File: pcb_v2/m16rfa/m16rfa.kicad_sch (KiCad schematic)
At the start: 51 parts, among them J1 S16A, J10 bus_rf16_3, J2 S16A, J3 SWRDA, J5 S16A, J6 S16A, J7 S16A, J8 bus_rf16_1, J9 bus_rf16_2, U1 74LS125, U10 74LS244, U11 74LS244, U2 74LS193, U3 74LS138, U4 74LS08, U5 74LS04, U6 74LS08, U7 74LS244, U8 74LS244, U9 74LS244

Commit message: recomeçando o roteamento
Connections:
- net +5V: now also U4.12, U4.13, U5.11, U5.13, U5.5, U5.9, U6.12, U6.13
- net data_{0}: now also J8.4 (Pin_4); no longer J8.14 (Pin_14)
- net data_{1}: now also J8.3 (Pin_3); no longer J8.13 (Pin_13)
- net data_{2}: now also J8.5 (Pin_5); no longer J8.11 (Pin_11)
- net data_{3}: now also J8.7 (Pin_7); no longer J8.9 (Pin_9)
- net data_{4}: now also J8.9 (Pin_9); no longer J8.7 (Pin_7)
- net data_{5}: now also J8.11 (Pin_11); no longer J8.5 (Pin_5)
- net data_{6}: now also J8.13 (Pin_13); no longer J8.3 (Pin_3)
- net data_{7}: now also J8.14 (Pin_14); no longer J8.4 (Pin_4)
- no-connect marks 74 -> 66

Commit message: .
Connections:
- net +5V: no longer U5.11, U5.9
- net pcia_swap: now also U5.8; no longer J9.3 (Pin_3)
- net pclr_swap: now also U5.10; no longer J9.1 (Pin_1)
- new net ~{pcia_swap}: J9.3 (Pin_3), U5.11
- new net ~{pclr_swap}: J9.1 (Pin_1), U5.9
- no-connect marks 66 -> 64
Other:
- moved on the sheet: U5D, U5E

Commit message: refazendo o módulo de registradores
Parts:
- removed J3: SWRDA, edge_connector:male-edge-connector-44, symbol Connector_Generic:Conn_02x22_Top_Bottom
- added C12, C13, C14, C15, C16, C17, C18, C19, C20, C21, C22, C23, C24, C25, C26, C27, C28, C29: 100nF, Capacitor_THT:C_Disc_D5.1mm_W3.2mm_P5.00mm, symbol Device:C
- added D10, D12, D14, D2, D4, D6, D8: RD, LED_THT:LED_D5.0mm, symbol Device:LED
- added D11, D13, D15, D3, D5, D7, D9: WR, LED_THT:LED_D5.0mm, symbol Device:LED
- added R20, R21, R22, R23, R25, R26, R27, R28, R29, R30, R31, R32, R33, R34: 1K, Resistor_THT:R_Axial_DIN0207_L6.3mm_D2.5mm_P7.62mm_Horizontal, symbol Device:R
- added U12, U15, U16, U17, U18, U19, U20: 74LS574, Package_DIP:DIP-20_W7.62mm, symbol 74xx:74LS574
- added U13: 74LS02, Package_DIP:DIP-14_W7.62mm, symbol 74xx:74LS02
- added U14: 74LS04, Package_DIP:DIP-14_W7.62mm, symbol 74xx:74LS04
- added U21: 74LS08, Package_DIP:DIP-14_W7.62mm, symbol 74xx:74LS08
- added U22, U23, U26, U27, U28, U29: 74LS138, Package_DIP:DIP-16_W7.62mm, symbol 74xx:74LS138
- added U24: 74LS32, Package_DIP:DIP-14_W7.62mm, symbol 74xx:74LS32
- added U25: 74LS00, Package_DIP:DIP-14_W7.62mm, symbol 74xx:74LS00
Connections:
- net +5V: now also C12.2, C13.2, C14.2, C15.2, C16.2, C17.2, C18.2, C19.2, C20.2, C21.2, C22.2, C23.2, C24.2, C25.2, C26.2, C27.2, C28.2, C29.2, D10.2 (A), D12.2 (A), D14.2 (A), D2.2 (A), D4.2 (A), D6.2 (A), D8.2 (A), U12.20 (VCC), U13.14 (VCC), U14.14 (VCC), U15.20 (VCC), U16.20 (VCC), U17.20 (VCC), U18.20 (VCC), U19.20 (VCC), U20.20 (VCC), U21.14 (VCC), U22.16 (VCC), U23.16 (VCC), U24.14 (VCC), U25.14 (VCC), U26.16 (VCC), U27.16 (VCC), U28.16 (VCC), U29.16 (VCC)
- net GND: now also C12.1, C13.1, C14.1, C15.1, C16.1, C17.1, C18.1, C19.1, C20.1, C21.1, C22.1, C23.1, C24.1, C25.1, C26.1, C27.1, C28.1, C29.1, D11.1 (K), D13.1 (K), D15.1 (K), D3.1 (K), D5.1 (K), D7.1 (K), D9.1 (K), U12.10 (GND), U13.7 (GND), U14.7 (GND), U15.10 (GND), U16.10 (GND), U17.10 (GND), U18.10 (GND), U19.10 (GND), U20.10 (GND), U21.7 (GND), U22.8 (GND), U23.8 (GND), U24.7 (GND), U25.7 (GND), U26.8 (GND), U27.8 (GND), U28.3 (A2), U28.8 (GND), U29.3 (A2), U29.8 (GND)
- net clock: now also U14.13, U21.2, U25.13, U25.5
- net mar_inc: now also U25.11
- net memory_read: now also U13.4
- net memory_write: now also U13.1
- net pc_inc: now also U25.6
- net rd_addr_0: now also U26.1 (A0), U27.1 (A0)
- net rd_addr_1: now also U26.2 (A1), U27.2 (A1), U29.1 (A0)
- net rd_addr_2: now also U26.3 (A2), U27.3 (A2), U29.2 (A1)
- net rd_addr_3: now also U14.5, U27.4 (E1), U27.5 (E2), U29.6 (E3)
- net rd_addr_4: now also U13.6, U26.6 (E3), U27.6 (E3), U29.4 (E1), U29.5 (E2)
- net sp_dec: now also U24.3
- net sp_inc: now also U24.6
- net wr_addr_0: now also U22.1 (A0), U23.1 (A0)
- net wr_addr_1: now also U22.2 (A1), U23.2 (A1), U28.1 (A0)
- net wr_addr_2: now also U22.3 (A2), U23.3 (A2), U28.2 (A1)
- net wr_addr_3: now also U14.1, U23.4 (E1), U23.5 (E2)
- net wr_addr_4: now also U13.3, U14.3, U23.6 (E3), U28.5 (E2)
- net wr_enable: now also U21.1, U28.6 (E3)
- net ~{addr_mar}: now also U21.8
- net ~{addr_pc}: now also U14.8
- net ~{addr_sp}: now also U21.11
- new net: D5.2 (A), R22.2
- new net: D6.1 (K), R28.2
- new net: D4.1 (K), R23.2
- new net: U14.11, U25.12, U25.8
- new net: D7.2 (A), R25.2
- new net: D8.1 (K), R31.2
- new net: U14.12, U24.2, U24.5
- new net: U14.9, U25.3, U25.4
- new net: U14.10, U21.10
- new net: D12.1 (K), R34.2
- new net: D15.2 (A), R29.2
- new net: D2.1 (K), R21.2
- new net: D9.2 (A), R30.2
- new net: D10.1 (K), R27.2
- new net: D14.1 (K), R32.2
- new net: D3.2 (A), R20.2
- new net: D11.2 (A), R26.2
- new net: D13.2 (A), R33.2
- new net: U21.6, U21.9
- new net data_0: U12.19 (Q0), U12.2 (D0), U15.19 (Q0), U15.2 (D0), U16.19 (Q0), U16.2 (D0), U17.19 (Q0), U17.2 (D0), U18.19 (Q0), U18.2 (D0), U19.19 (Q0), U19.2 (D0), U20.19 (Q0), U20.2 (D0)
- new net data_1: U12.18 (Q1), U12.3 (D1), U15.18 (Q1), U15.3 (D1), U16.18 (Q1), U16.3 (D1), U17.18 (Q1), U17.3 (D1), U18.18 (Q1), U18.3 (D1), U19.18 (Q1), U19.3 (D1), U20.18 (Q1), U20.3 (D1)
- new net data_2: U12.17 (Q2), U12.4 (D2), U15.17 (Q2), U15.4 (D2), U16.17 (Q2), U16.4 (D2), U17.17 (Q2), U17.4 (D2), U18.17 (Q2), U18.4 (D2), U19.17 (Q2), U19.4 (D2), U20.17 (Q2), U20.4 (D2)
- new net data_3: U12.16 (Q3), U12.5 (D3), U15.16 (Q3), U15.5 (D3), U16.16 (Q3), U16.5 (D3), U17.16 (Q3), U17.5 (D3), U18.16 (Q3), U18.5 (D3), U19.16 (Q3), U19.5 (D3), U20.16 (Q3), U20.5 (D3)
- new net data_4: U12.15 (Q4), U12.6 (D4), U15.15 (Q4), U15.6 (D4), U16.15 (Q4), U16.6 (D4), U17.15 (Q4), U17.6 (D4), U18.15 (Q4), U18.6 (D4), U19.15 (Q4), U19.6 (D4), U20.15 (Q4), U20.6 (D4)
- new net data_5: U12.14 (Q5), U12.7 (D5), U15.14 (Q5), U15.7 (D5), U16.14 (Q5), U16.7 (D5), U17.14 (Q5), U17.7 (D5), U18.14 (Q5), U18.7 (D5), U19.14 (Q5), U19.7 (D5), U20.14 (Q5), U20.7 (D5)
- new net data_6: U12.13 (Q6), U12.8 (D6), U15.13 (Q6), U15.8 (D6), U16.13 (Q6), U16.8 (D6), U17.13 (Q6), U17.8 (D6), U18.13 (Q6), U18.8 (D6), U19.13 (Q6), U19.8 (D6), U20.13 (Q6), U20.8 (D6)
- new net data_7: U12.12 (Q7), U12.9 (D7), U15.12 (Q7), U15.9 (D7), U16.12 (Q7), U16.9 (D7), U17.12 (Q7), U17.9 (D7), U18.12 (Q7), U18.9 (D7), U19.12 (Q7), U19.9 (D7), U20.12 (Q7), U20.9 (D7)
- new net write: U21.3, U22.6 (E3)
- new net write_A: R20.1, U12.11 (Cp)
- new net write_B: R22.1, U15.11 (Cp)
- new net write_C: R25.1, U16.11 (Cp)
- new net write_D: R30.1, U18.11 (Cp)
- new net write_E: R26.1, U20.11 (Cp)
- new net write_H: R33.1, U17.11 (Cp)
- new net write_L: R29.1, U19.11 (Cp)
- new net ~{addr_read_mar}: U25.10, U29.13 (O2)
- new net ~{addr_read_pc}: U25.2, U29.15 (O0)
- new net ~{addr_read_sp}: U21.13, U24.4, U29.14 (O1)
- new net ~{addr_write_mar}: U25.9, U28.13 (O2)
- new net ~{addr_write_pc}: U25.1, U28.15 (O0)
- new net ~{addr_write_sp}: U21.12, U24.1, U28.14 (O1)
- new net ~{rd_addr_3}: U13.5, U14.6, U26.4 (E1), U26.5 (E2)
- new net ~{read_A}: R21.1, U12.1 (OE)
- new net ~{read_B}: R23.1, U15.1 (OE)
- new net ~{read_C}: R28.1, U16.1 (OE)
- new net ~{read_D}: R31.1, U18.1 (OE)
- new net ~{read_E}: R27.1, U20.1 (OE)
- new net ~{read_H}: R34.1, U17.1 (OE)
- new net ~{read_L}: R32.1, U19.1 (OE)
- new net ~{read_iod_mar}: U21.5, U27.15 (O0)
- new net ~{sel_read_lrh}: U26.7 (O7)
- new net ~{sel_read_lrl}: U26.9 (O6)
- new net ~{sel_read_marh}: U26.10 (O5)
- new net ~{sel_read_marl}: U26.11 (O4)
- new net ~{sel_read_pch}: U26.14 (O1)
- new net ~{sel_read_pcl}: U26.15 (O0)
- new net ~{sel_read_sph}: U26.12 (O3)
- new net ~{sel_read_spl}: U26.13 (O2)
- new net ~{sel_write_lrh}: U22.7 (O7)
- new net ~{sel_write_lrl}: U22.9 (O6)
- new net ~{sel_write_marh}: U22.10 (O5)
- new net ~{sel_write_marl}: U22.11 (O4)
- new net ~{sel_write_pch}: U22.14 (O1)
- new net ~{sel_write_pcl}: U22.15 (O0)
- new net ~{sel_write_sph}: U22.12 (O3)
- new net ~{sel_write_spl}: U22.13 (O2)
- new net ~{wr_addr_3}: U13.2, U14.2, U22.4 (E1), U28.4 (E1)
- new net ~{wr_addr_4}: U14.4, U22.5 (E2)
- new net ~{write_iod_mar}: U21.4, U23.15 (O0)
- no-connect marks 64 -> 97
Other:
- moved on the sheet: C1, C4, C5, C6, C7, C8, C9, D1, R19, U1E, U4D, U4E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

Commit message: Redimensionamento do clock para abrir mais espaço para os registradores
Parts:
- removed C12, C15, C16, C17, C18, C19, C20: 100nF, Capacitor_THT:C_Disc_D5.1mm_W3.2mm_P5.00mm, symbol Device:C
- removed D10, D12, D14, D2, D4, D6, D8: RD, LED_THT:LED_D5.0mm, symbol Device:LED
- removed D11, D13, D15, D3, D5, D7, D9: WR, LED_THT:LED_D5.0mm, symbol Device:LED
- removed R20, R21, R22, R23, R25, R26, R27, R28, R29, R30, R31, R32, R33, R34: 1K, Resistor_THT:R_Axial_DIN0207_L6.3mm_D2.5mm_P7.62mm_Horizontal, symbol Device:R
- removed U12, U15, U16, U17, U18, U19, U20: 74LS574, Package_DIP:DIP-20_W7.62mm, symbol 74xx:74LS574
- added J3: SR8A, edge_connector:male-edge-connector-44, symbol Connector_Generic:Conn_02x22_Top_Bottom
- renumbered D1 to D15
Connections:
- net ~{sel_read_lrh} is gone; now on net ~{read_lrh}: U26.7 (O7)
- net ~{sel_read_lrl} is gone; now on net ~{read_lrl}: U26.9 (O6)
- net ~{sel_read_marh} is gone; now on net ~{read_marh}: U26.10 (O5)
- net ~{sel_read_marl} is gone; now on net ~{read_marl}: U26.11 (O4)
- net ~{sel_read_pch} is gone; now on net ~{read_pch}: U26.14 (O1)
- net ~{sel_read_pcl} is gone; now on net ~{read_pcl}: U26.15 (O0)
- net ~{sel_read_sph} is gone; now on net ~{read_sph}: U26.12 (O3)
- net ~{sel_read_spl} is gone; now on net ~{read_spl}: U26.13 (O2)
- net ~{sel_write_lrh} is gone; now on net ~{write_lrh}: U22.7 (O7)
- net ~{sel_write_lrl} is gone; now on net ~{write_lrl}: U22.9 (O6)
- net ~{sel_write_marh} is gone; now on net ~{write_marh}: U22.10 (O5)
- net ~{sel_write_marl} is gone; now on net ~{write_marl}: U22.11 (O4)
- net ~{sel_write_pch} is gone; now on net ~{write_pch}: U22.14 (O1)
- net ~{sel_write_pcl} is gone; now on net ~{write_pcl}: U22.15 (O0)
- net ~{sel_write_sph} is gone; now on net ~{write_sph}: U22.12 (O3)
- net ~{sel_write_spl} is gone; now on net ~{write_spl}: U22.13 (O2)
- net +5V: now also U13.11, U13.12, U13.8, U13.9, U24.10, U24.12, U24.13, U24.9, J3.1 (Pin_1), J3.23 (Pin_23)
- net GND: now also J3.22 (Pin_22), J3.44 (Pin_44)
- net clock: now also J3.43 (Pin_43)
- net data_{0}: now also J3.34 (Pin_34)
- net data_{1}: now also J3.35 (Pin_35)
- net data_{2}: now also J3.36 (Pin_36)
- net data_{3}: now also J3.37 (Pin_37)
- net data_{4}: now also J3.38 (Pin_38)
- net data_{5}: now also J3.39 (Pin_39)
- net data_{6}: now also J3.40 (Pin_40)
- net data_{7}: now also J3.41 (Pin_41)
- net rd_addr_0: now also J3.29 (Pin_29)
- net rd_addr_1: now also J3.30 (Pin_30)
- net rd_addr_2: now also J3.31 (Pin_31)
- net rd_addr_3: now also J3.33 (Pin_33)
- net rd_addr_4: now also J3.32 (Pin_32)
- net wr_addr_0: now also J3.24 (Pin_24)
- net wr_addr_1: now also J3.25 (Pin_25)
- net wr_addr_2: now also J3.26 (Pin_26)
- net wr_addr_3: now also J3.27 (Pin_27)
- net wr_addr_4: now also J3.28 (Pin_28)
- net wr_enable: now also J3.42 (Pin_42)
- no-connect marks 97 -> 109
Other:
- moved on the sheet: C1, C10, C11, C13, C14, C2, C21, C22, C23, C24, C25, C26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

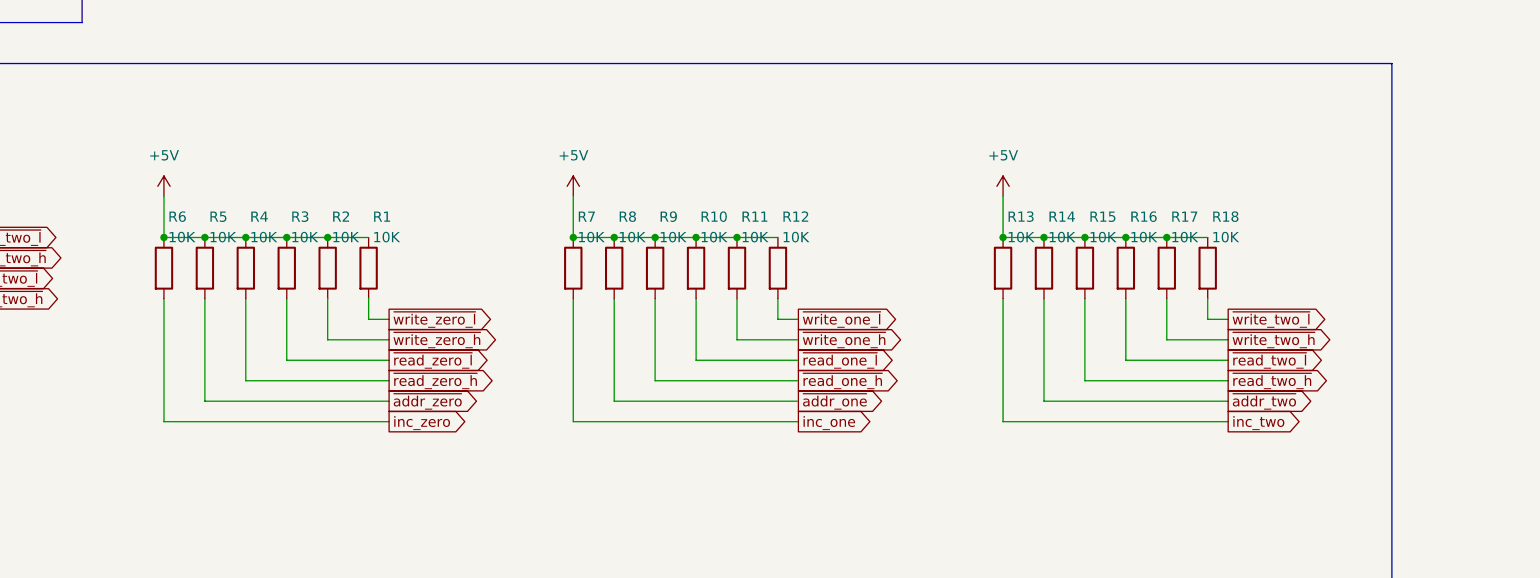
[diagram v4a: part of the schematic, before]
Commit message: atualização do conector flat
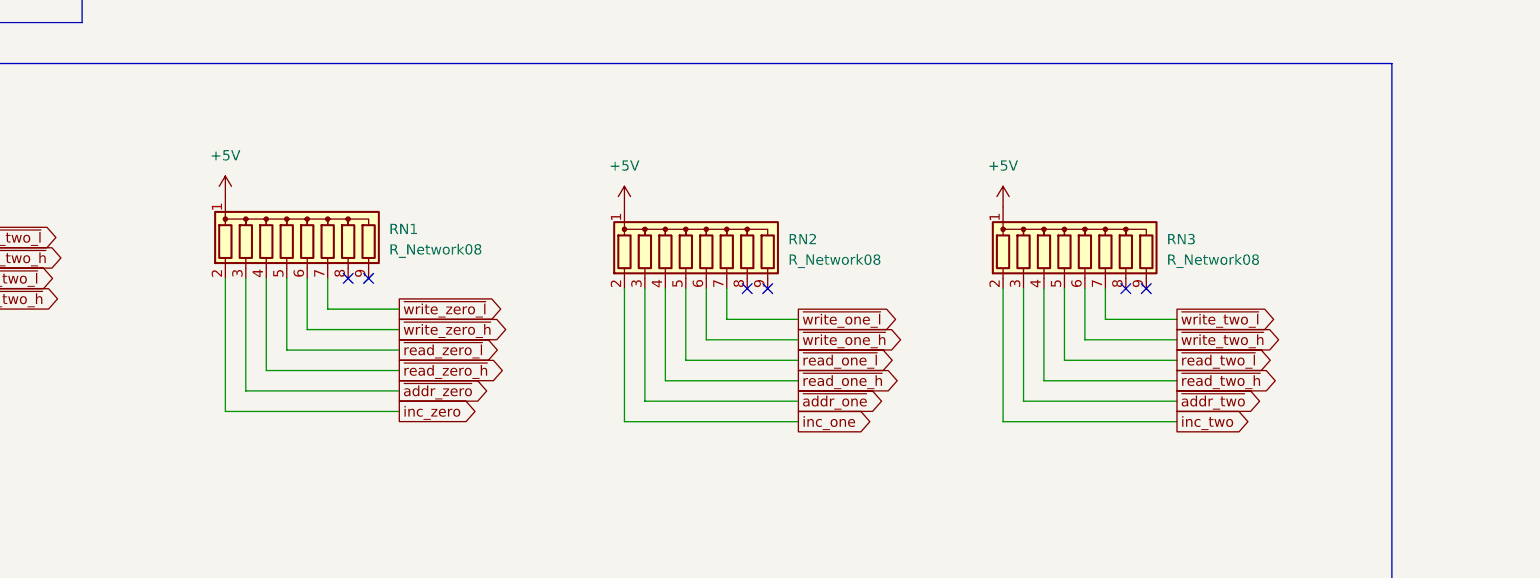
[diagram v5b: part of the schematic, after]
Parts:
- removed R1, R10, R11, R12, R13, R14, R15, R16, R17, R18, R2, R3, R4, R5, R6, R7, R8, R9: 10K, Resistor_THT:R_Axial_DIN0207_L6.3mm_D2.5mm_P7.62mm_Horizontal, symbol Device:R
- added RN1, RN2, RN3: R_Network08, Resistor_THT:R_Array_SIP9, symbol Device:R_Network08
- J10, J8, J9: footprint Connector_PinHeader_2.54mm:PinHeader_2x08_P2.54mm_Vertical -> edge_connector:conector 02x08
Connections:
- net +5V: now also RN1.1 (common), RN2.1 (common), RN3.1 (common)
- net inc_one: now also RN2.2 (R1)
- net inc_two: now also RN3.2 (R1)
- net inc_zero: now also RN1.2 (R1)
- net ~{addr_one}: now also RN2.3 (R2)
- net ~{addr_two}: now also RN3.3 (R2)
- net ~{addr_zero}: now also RN1.3 (R2)
- net ~{read_one_h}: now also RN2.4 (R3)
- net ~{read_one_l}: now also RN2.5 (R4)
- net ~{read_two_h}: now also RN3.4 (R3)
- net ~{read_two_l}: now also RN3.5 (R4)
- net ~{read_zero_h}: now also RN1.4 (R3)
- net ~{read_zero_l}: now also RN1.5 (R4)
- net ~{write_one_h}: now also RN2.6 (R5)
- net ~{write_one_l}: now also RN2.7 (R6)
- net ~{write_two_h}: now also RN3.6 (R5)
- net ~{write_two_l}: now also RN3.7 (R6)
- net ~{write_zero_h}: now also RN1.6 (R5)
- net ~{write_zero_l}: now also RN1.7 (R6)
- no-connect marks 109 -> 115

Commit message: .
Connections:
- net clock: now also J3.12 (Pin_12); no longer J3.43 (Pin_43)
- net data_{0}: now also J3.24 (Pin_24); no longer J3.34 (Pin_34)
- net data_{1}: now also J3.25 (Pin_25); no longer J3.35 (Pin_35)
- net data_{2}: now also J3.26 (Pin_26); no longer J3.36 (Pin_36)
- net data_{3}: now also J3.27 (Pin_27); no longer J3.37 (Pin_37)
- net data_{4}: now also J3.28 (Pin_28); no longer J3.38 (Pin_38)
- net data_{5}: now also J3.29 (Pin_29); no longer J3.39 (Pin_39)
- net data_{6}: now also J3.30 (Pin_30); no longer J3.40 (Pin_40)
- net data_{7}: now also J3.31 (Pin_31); no longer J3.41 (Pin_41)
- net rd_addr_0: now also J3.38 (Pin_38); no longer J3.29 (Pin_29)
- net rd_addr_1: now also J3.39 (Pin_39); no longer J3.30 (Pin_30)
- net rd_addr_2: now also J3.40 (Pin_40); no longer J3.31 (Pin_31)
- net rd_addr_3: now also J3.42 (Pin_42); no longer J3.33 (Pin_33)
- net rd_addr_4: now also J3.41 (Pin_41); no longer J3.32 (Pin_32)
- net wr_addr_0: now also J3.17 (Pin_17); no longer J3.24 (Pin_24)
- net wr_addr_1: now also J3.18 (Pin_18); no longer J3.25 (Pin_25)
- net wr_addr_2: now also J3.19 (Pin_19); no longer J3.26 (Pin_26)
- net wr_addr_3: now also J3.20 (Pin_20); no longer J3.27 (Pin_27)
- net wr_addr_4: now also J3.21 (Pin_21); no longer J3.28 (Pin_28)
- net wr_enable: now also J3.43 (Pin_43); no longer J3.42 (Pin_42)

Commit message: concluido o novo layout
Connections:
- net +5V: now also U11.11 (I0b), U11.13 (I1b), U11.15 (I2b), U11.17 (I3b), U7.15 (I2b), U7.17 (I3b), U8.15 (I2b), U8.17 (I3b), U9.15 (I2b), U9.17 (I3b)
- net GND: no longer U11.11 (I0b), U11.13 (I1b), U11.15 (I2b), U11.17 (I3b), U7.15 (I2b), U7.17 (I3b), U8.15 (I2b), U8.17 (I3b), U9.15 (I2b), U9.17 (I3b)
- net inc_two: now also RN3.7 (R6); no longer RN3.2 (R1)
- net inc_zero: now also RN1.5 (R4); no longer RN1.2 (R1)
- net ~{addr_two}: now also RN3.8 (R7); no longer RN3.3 (R2)
- net ~{addr_zero}: now also RN1.9 (R8); no longer RN1.3 (R2)
- net ~{read_two_h}: now also RN3.9 (R8); no longer RN3.4 (R3)
- net ~{read_two_l}: now also RN3.6 (R5); no longer RN3.5 (R4)
- net ~{read_zero_l}: now also RN1.7 (R6); no longer RN1.5 (R4)
- net ~{write_one_h}: now also RN2.7 (R6); no longer RN2.6 (R5)
- net ~{write_one_l}: now also RN2.6 (R5); no longer RN2.7 (R6)
- net ~{write_two_h}: now also RN3.5 (R4); no longer RN3.6 (R5)
- net ~{write_two_l}: now also RN3.2 (R1); no longer RN3.7 (R6)
- net ~{write_zero_h}: now also RN1.8 (R7); no longer RN1.6 (R5)
- net ~{write_zero_l}: now also RN1.6 (R5); no longer RN1.7 (R6)
